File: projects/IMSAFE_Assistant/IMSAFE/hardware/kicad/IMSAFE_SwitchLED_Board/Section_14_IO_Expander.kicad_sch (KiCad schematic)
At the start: 0 parts

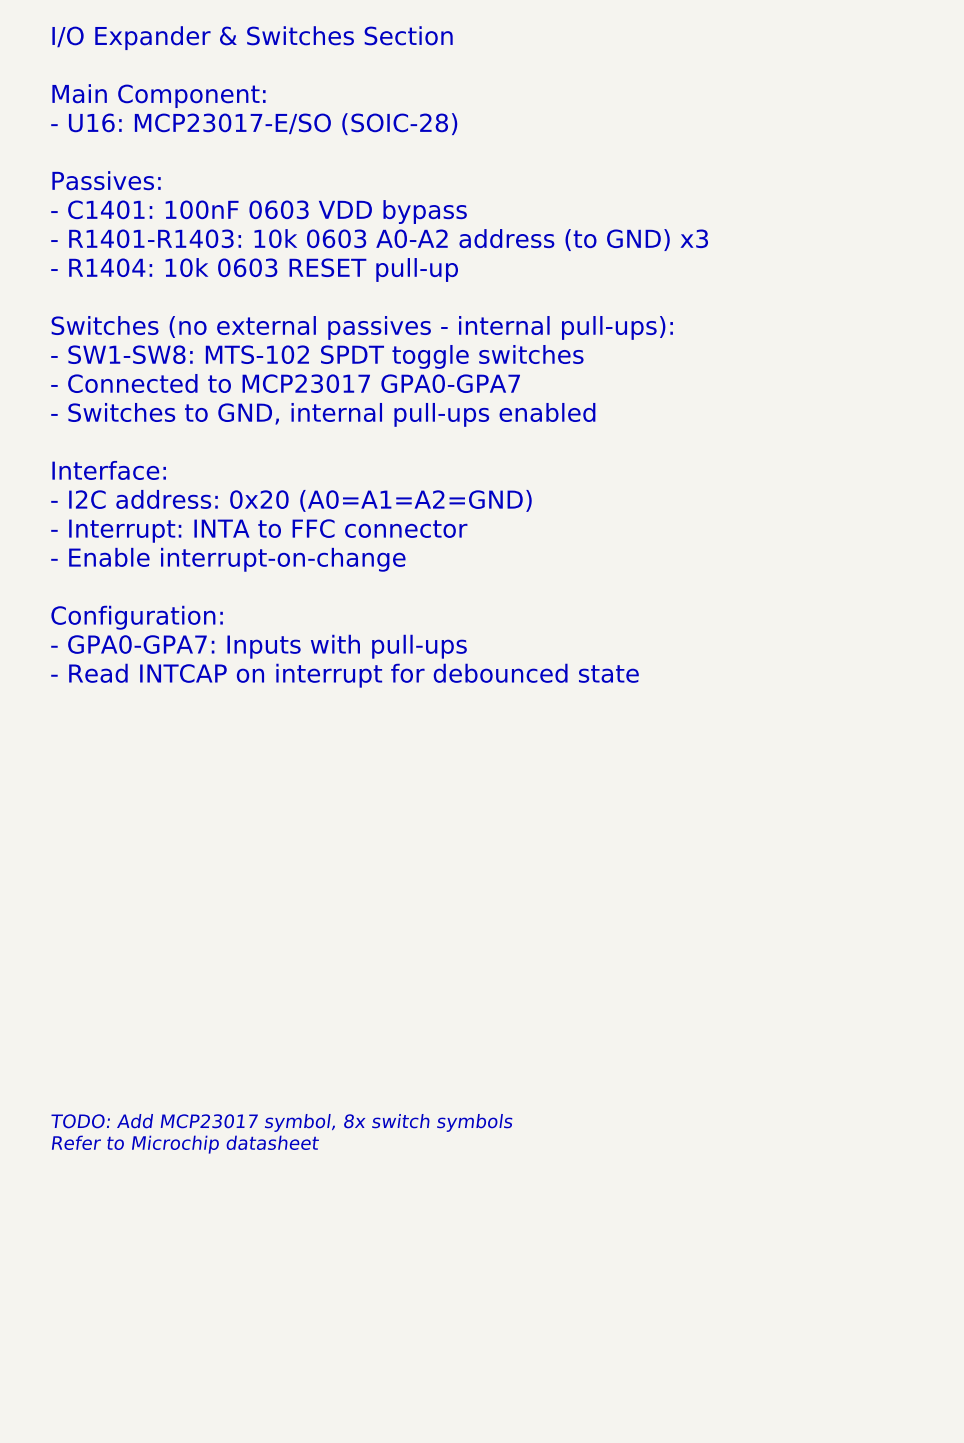
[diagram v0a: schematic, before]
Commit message: Update KiCad schematics and add analysis files
- Update all MainBoard schematic sections with component placement
- Add ERC reports and analysis scripts for schematic validation
- Update Radar Interface and SwitchLED Board projects
- Sync KiCad project files with latest session changes

Co-Authored-By: Claude Opus 4.5 <noreply@anthropic.com>
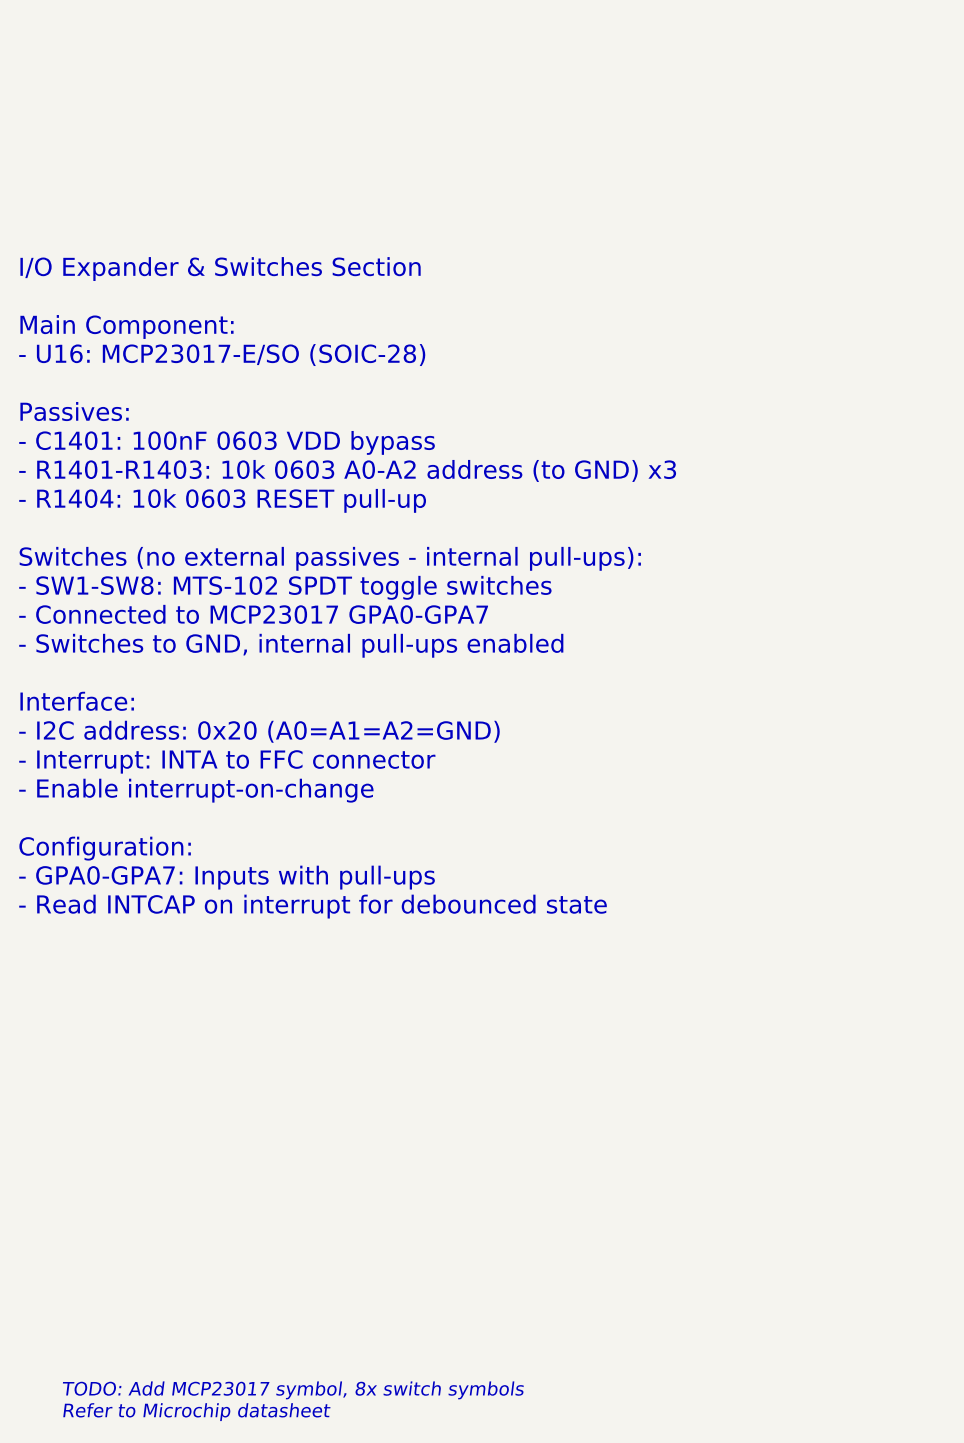
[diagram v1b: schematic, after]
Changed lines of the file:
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@@
 (kicad_sch
-	(version 20231120)
+	(version 20250114)
 	(generator "eeschema")
-	(generator_version "8.0")
-	(uuid "sec14-0001-0002-0003-000000000001")
+	(generator_version "9.0")
 	(paper "A4")
 	(title_block
@@
 		(comment 2 "8x Toggle Switches")
 	)
-	(text "I/O Expander & Switches Section\n\nMain Component:\n- U16: MCP23017-E/SO (SOIC-28)\n\nPassives:\n- C1401: 100nF 0603 VDD bypass\n- R1401-R1403: 10k 0603 A0-A2 address (to GND) x3\n- R1404: 10k 0603 RESET pull-up\n\nSwitches (no external passives - internal pull-ups):\n- SW1-SW8: MTS-102 SPDT toggle switches\n- Connected to MCP23017 GPA0-GPA7\n- Switches to GND, internal pull-ups enabled\n\nInterface:\n- I2C address: 0x20 (A0=A1=A2=GND)\n- Interrupt: INTA to FFC connector\n- Enable interrupt-on-change\n\nConfiguration:\n- GPA0-GPA7: Inputs with pull-ups\n- Read INTCAP on interrupt for debounced state"
-		(exclude_from_sim no)
-		(at 25.4 25.4 0)
-		(effects
-			(font
-				(size 2 2)
-			)
-			(justify left)
-		)
-		(uuid "sec14-text-001")
-	)
 	(text "TODO: Add MCP23017 symbol, 8x switch symbols\nRefer to Microchip datasheet"
 		(exclude_from_sim no)
-		(at 25.4 111.76 0)
+		(at 26.67 141.478 0)
 		(effects
 			(font
@@
 			(justify left)
 		)
-		(uuid "sec14-todo-001")
+	)
+	(text "I/O Expander & Switches Section\n\nMain Component:\n- U16: MCP23017-E/SO (SOIC-28)\n\nPassives:\n- C1401: 100nF 0603 VDD bypass\n- R1401-R1403: 10k 0603 A0-A2 address (to GND) x3\n- R1404: 10k 0603 RESET pull-up\n\nSwitches (no external passives - internal pull-ups):\n- SW1-SW8: MTS-102 SPDT toggle switches\n- Connected to MCP23017 GPA0-GPA7\n- Switches to GND, internal pull-ups enabled\n\nInterface:\n- I2C address: 0x20 (A0=A1=A2=GND)\n- Interrupt: INTA to FFC connector\n- Enable interrupt-on-change\n\nConfiguration:\n- GPA0-GPA7: Inputs with pull-ups\n- Read INTCAP on interrupt for debounced state"
+		(exclude_from_sim no)
+		(at 21.844 51.054 0)
+		(effects
+			(font
+				(size 2 2)
+			)
+			(justify left)
+		)
 	)
 )
